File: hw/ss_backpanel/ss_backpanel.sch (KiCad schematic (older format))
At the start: 16 parts, among them J101 4mm_banana_socket-LB_I4R_A-pa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, M101 Amphenol_T3437000-DIN7_panel_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, M102 Amphenol_T3437000-DIN7_panel_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, M103 Schurter-3101_0060-fuse_holde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, M104 FN283-1-06_Schaffner_AC-panel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, M105 74980104400-Wurth_RJ45-Panel_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, M106 TE-1734346-Panel_cutout, M107 CUI-UJ2_AH_1_SMT-Panel_cutout, M108 DSub9-Kycon_K22X-E9P-N-panel_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, M109 SJ-3571N_CUI_audio_jacket_pan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

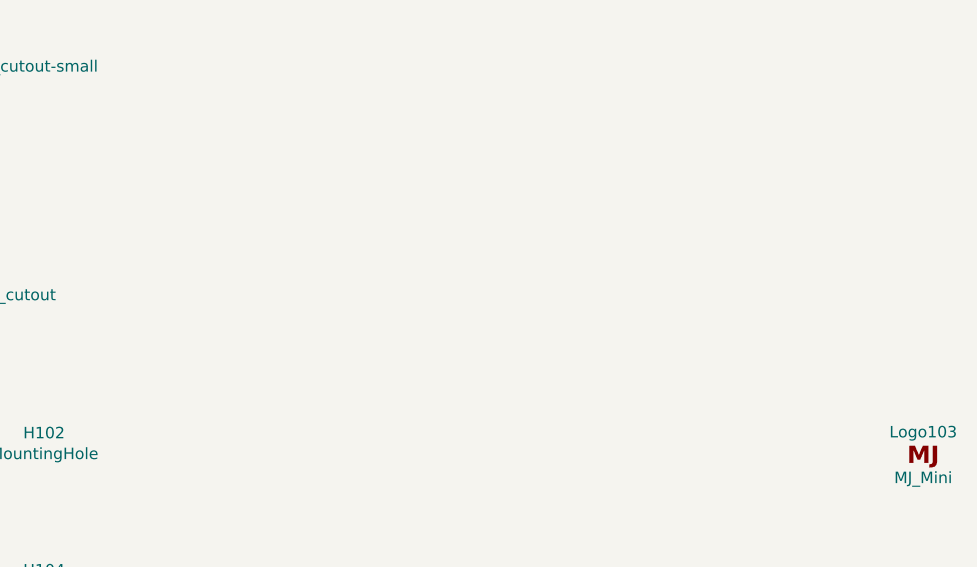
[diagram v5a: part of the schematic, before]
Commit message: Add 12V DC-out (Molex Nano-Fit 1x02) and SMA in back-panel, for FM antenna & ext. ant.amp. Updated Dsub9 conn to correct component & placement on MB.
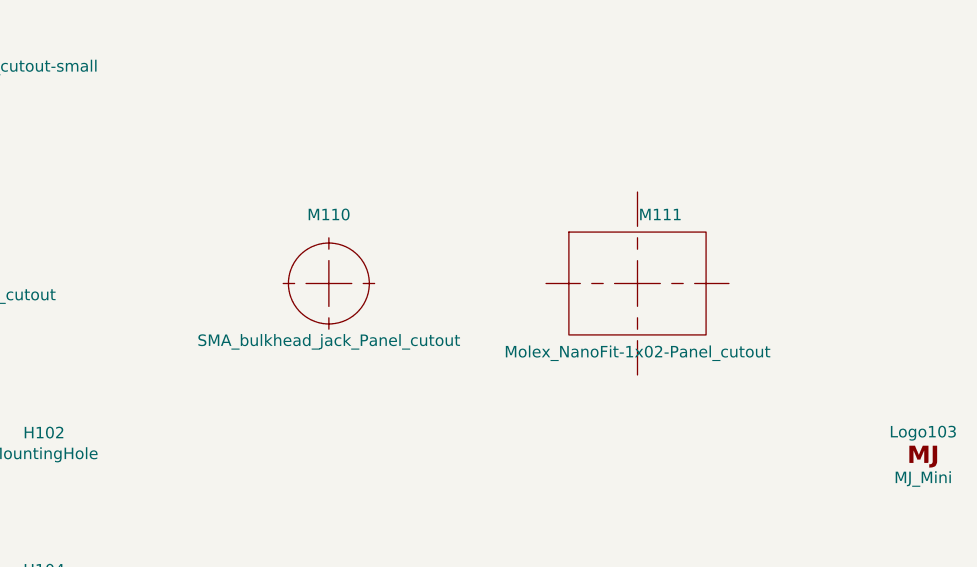
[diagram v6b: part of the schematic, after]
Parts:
- added M110: SMA_bulkhead_jack_Panel_cutout, customlib_mj_fp:SMA_Bulkhead_jack-Panel_cutout, symbol customlib_mj:SMA_bulkhead_jack_Panel_cutout
- added M111: Molex_NanoFit-1x02-Panel_cutout, customlib_mj_fp:Molex_NanoFit-1x02-Panel_cutout, symbol customlib_mj:Molex_NanoFit-1x02-Panel_cutout
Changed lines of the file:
@@
+	1    0    0    -1
+$EndComp
+$Comp
+L customlib_mj:SMA_bulkhead_jack_Panel_cutout M110
+U 1 1 5F881BCE
+P 7500 6000
+F 0 "M110" H 7500 6300 50  0000 C CNN
+F 1 "SMA_bulkhead_jack_Panel_cutout" H 7500 5750 50  0000 C CNN
+F 2 "customlib_mj_fp:SMA_Bulkhead_jack-Panel_cutout" H 7500 6000 50  0001 C CNN
+F 3 "" H 7500 6000 50  0001 C CNN
+	1    7500 6000
+	1    0    0    -1
+$EndComp
+$Comp
+L customlib_mj:Molex_NanoFit-1x02-Panel_cutout M111
+U 1 1 5F88251B
+P 8850 6000
+F 0 "M111" H 8950 6300 50  0000 C CNN
+F 1 "Molex_NanoFit-1x02-Panel_cutout" H 8850 5700 50  0000 C CNN
+F 2 "customlib_mj_fp:Molex_NanoFit-1x02-Panel_cutout" H 8850 6000 50  0001 C CNN
+F 3 "" H 8850 6000 50  0001 C CNN
+	1    8850 6000
 	1    0    0    -1
 $EndComp
